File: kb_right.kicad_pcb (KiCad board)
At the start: 2 copper layers, 3.4 x 3 mm, 171 parts, among them J1 10029449-001RLF, SW0 RotaryEncoder_Switch

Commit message: added smd caps
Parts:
- C101, C102, C103, C104, C105, C106, C107, C108, C109, C110, C111, C112, C113, C114, C115, C116, C117, C118, C119, C120, C121, C122, C123, C124, C125, C126, C127, C128, C129, C130, C131, C132, C133, C134, C135, C136, C137, C138, C139, C140, C141, C142, D0, D1, D10, D101, D102, D103, D104, D105, D106, D107, D108, D109, D11, D110, D111, D112, D113, D114, D115, D116, D117, D118, D119, D12, D120, D121, D122, D123, D124, D125, D126, D127, D128, D129, D13, D130, D131, D132, D133, D134, D135, D136, D137, D138, D139, D14, D140, D141, D142, D15, D16, D17, D18, D19, D2, D20, D21, D22, D23, D24, D25, D26, D27, D28, D29, D3, D30, D31, D32, D33, D34, D35, D36, D37, D38, D39, D4, D40, D41, D42, D5, D6, D7, D8, D9: moved to B.Cu
- moved C101 508.5 mm to (27.8, 77.8), turned to -90 degrees
- moved C128 503.6 mm to (32.5, 134.9), turned to -90 degrees
- moved D9 476.8 mm to (30.2, 94.5), turned to 90 degrees
- moved D28 474.9 mm to (63.5, 132.6), turned to 90 degrees
- moved C135 466.6 mm to (36.5, 154.0), turned to -90 degrees
- moved C120 465.9 mm to (41.3, 115.9), turned to -90 degrees
- moved C111 456.5 mm to (55.6, 96.8), turned to -90 degrees
- moved D36 453.8 mm to (75.4, 151.6), turned to 90 degrees
- moved C109 449.3 mm to (18.3, 94.5), turned to 90 degrees
- moved C138 447.9 mm to (110.3, 154.0), turned to -90 degrees
- moved C102 446.2 mm to (46.0, 77.8), turned to -90 degrees
- moved C119 444.2 mm to (23.0, 113.5), turned to 90 degrees
- moved D3 434.0 mm to (77.8, 75.4), turned to 90 degrees
- moved D18 427.0 mm to (34.9, 113.5), turned to 90 degrees
- moved D12 425.5 mm to (87.3, 94.5), turned to 90 degrees
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
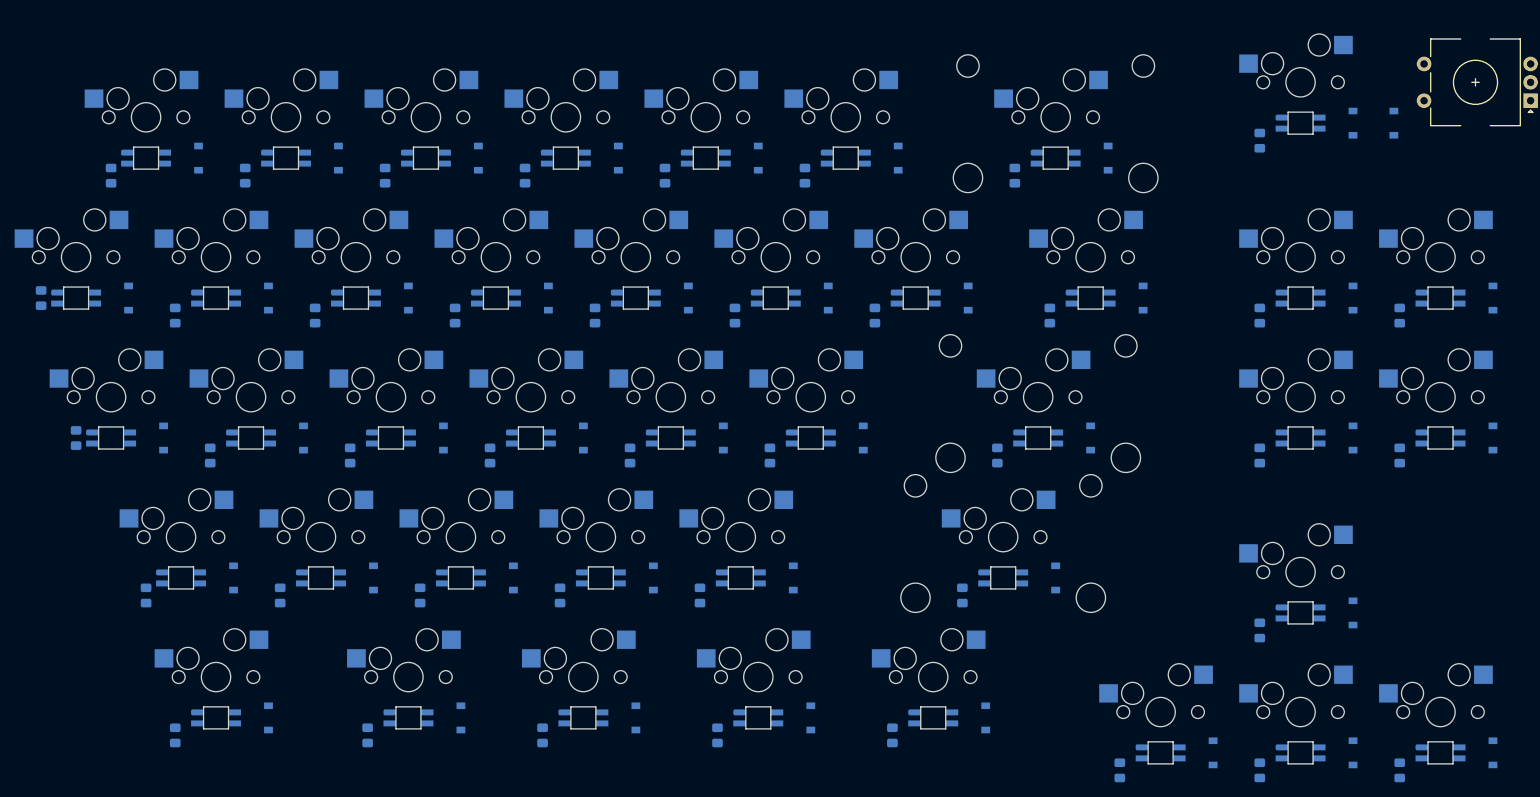
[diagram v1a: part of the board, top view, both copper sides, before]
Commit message: routed matrix
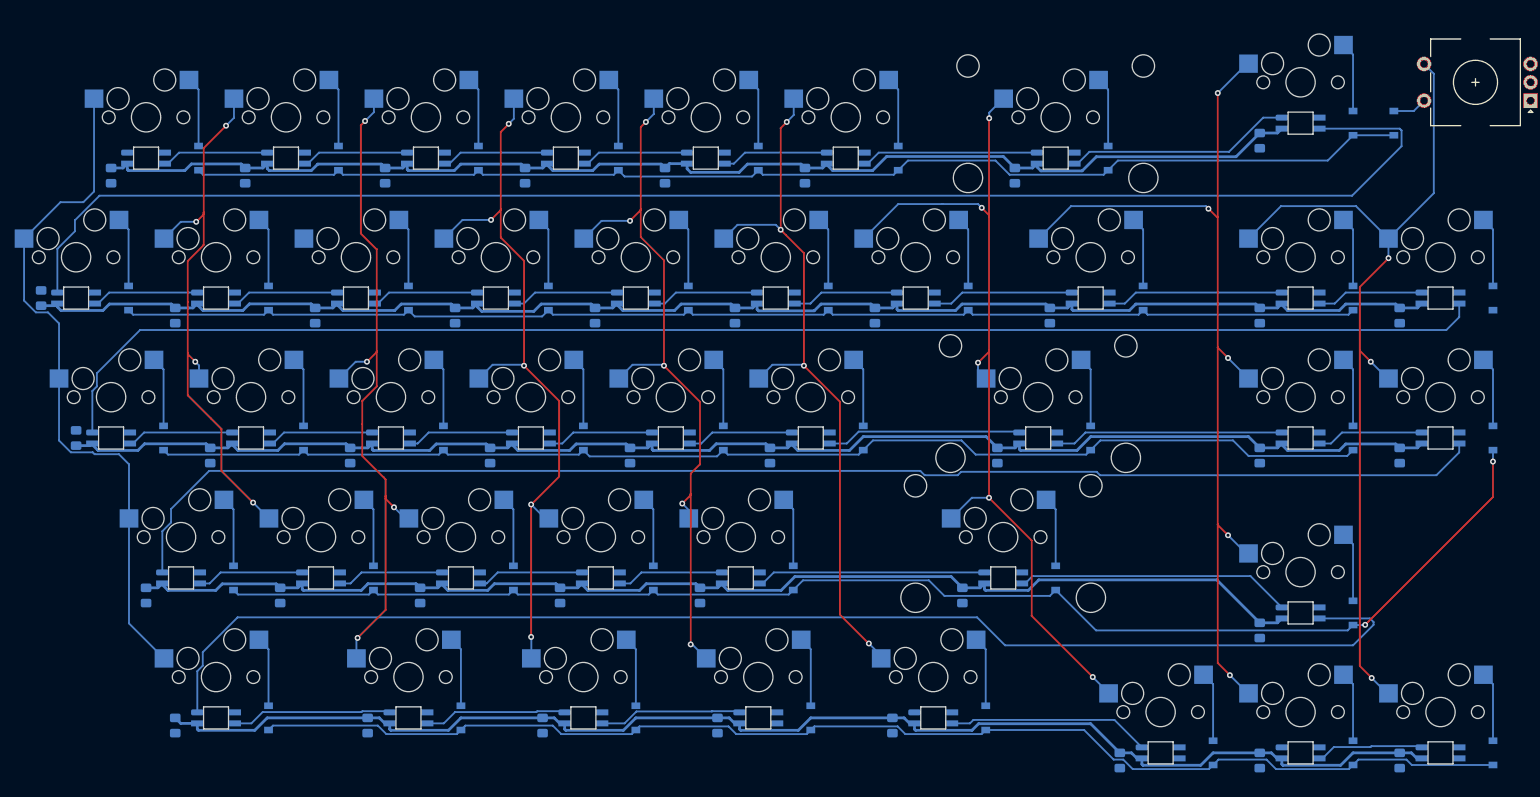
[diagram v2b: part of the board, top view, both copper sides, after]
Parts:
- moved C135 1.34 mm to (36.5, 152.6)
- moved C136 1.34 mm to (62.7, 152.6)
- moved C137 1.34 mm to (86.5, 152.6)
- moved C138 1.34 mm to (110.3, 152.6)
- moved C139 1.34 mm to (134.1, 152.6)
- moved C140 1.34 mm to (165.1, 157.4)
- moved C141 1.34 mm to (184.2, 157.4)
- moved C142 1.34 mm to (203.2, 157.4)
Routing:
- net +5V: track 0.00 -> 922.4 mm
- net Net-(D108-Pad1): track 0.00 -> 209.0 mm
- net Net-(D118-Pad1): track 0.00 -> 198.8 mm
- net /ROW8: track 0.00 -> 191.4 mm, vias 0 -> 2
- net Net-(D127-Pad1): track 0.00 -> 189.8 mm
- net Net-(D134-Pad1): track 0.00 -> 180.6 mm
- net /ROW9: track 0.00 -> 174.5 mm
- net /ROW6: track 0.00 -> 170.9 mm
- net /ROW5: track 0.00 -> 169.0 mm
- net /ROW7: track 0.00 -> 168.0 mm
- net /COL7: track 0.00 -> 128.1 mm, vias 0 -> 5
- net /COL8: track 0.00 -> 120.4 mm, vias 0 -> 3
- net /COL6: track 0.00 -> 119.6 mm, vias 0 -> 5
- net /COL4: track 0.00 -> 102.4 mm, vias 0 -> 5
- net /COL3: track 0.00 -> 101.5 mm, vias 0 -> 5
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
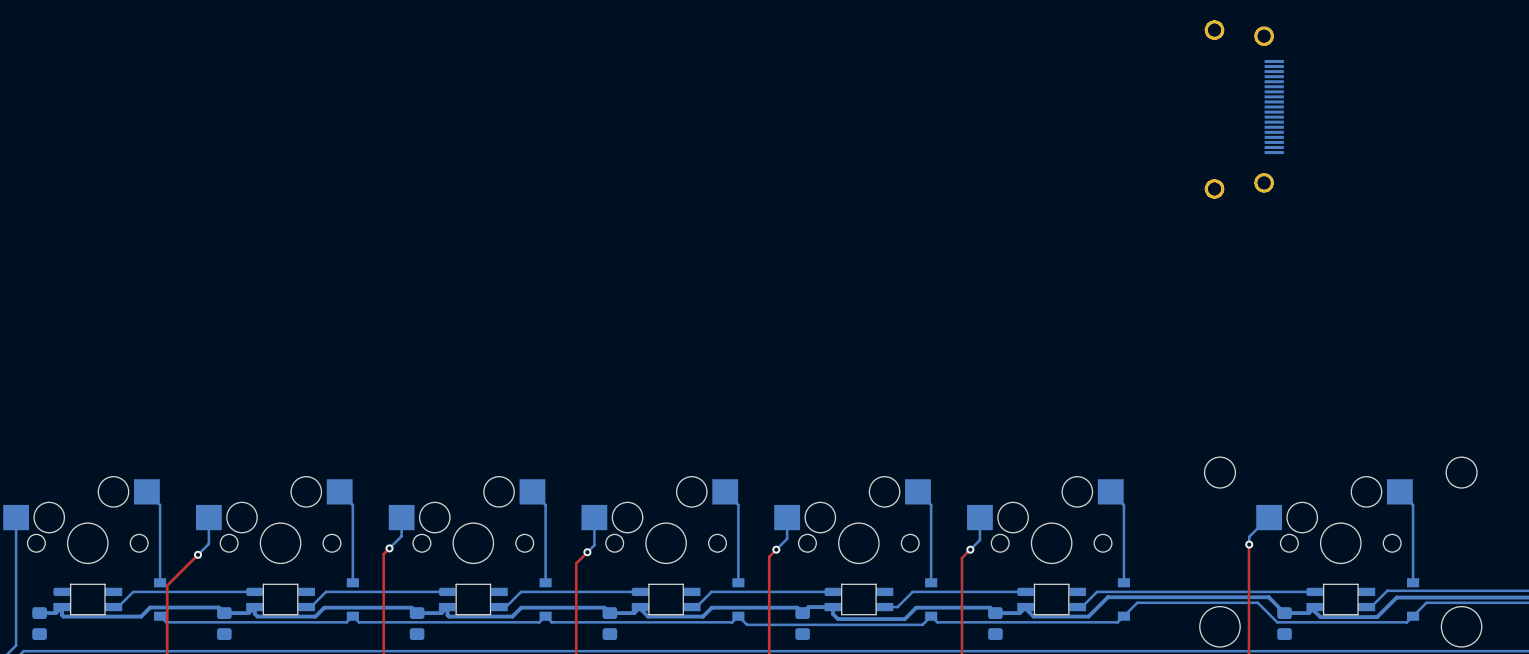
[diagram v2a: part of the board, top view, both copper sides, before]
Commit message: labelled hdmi port
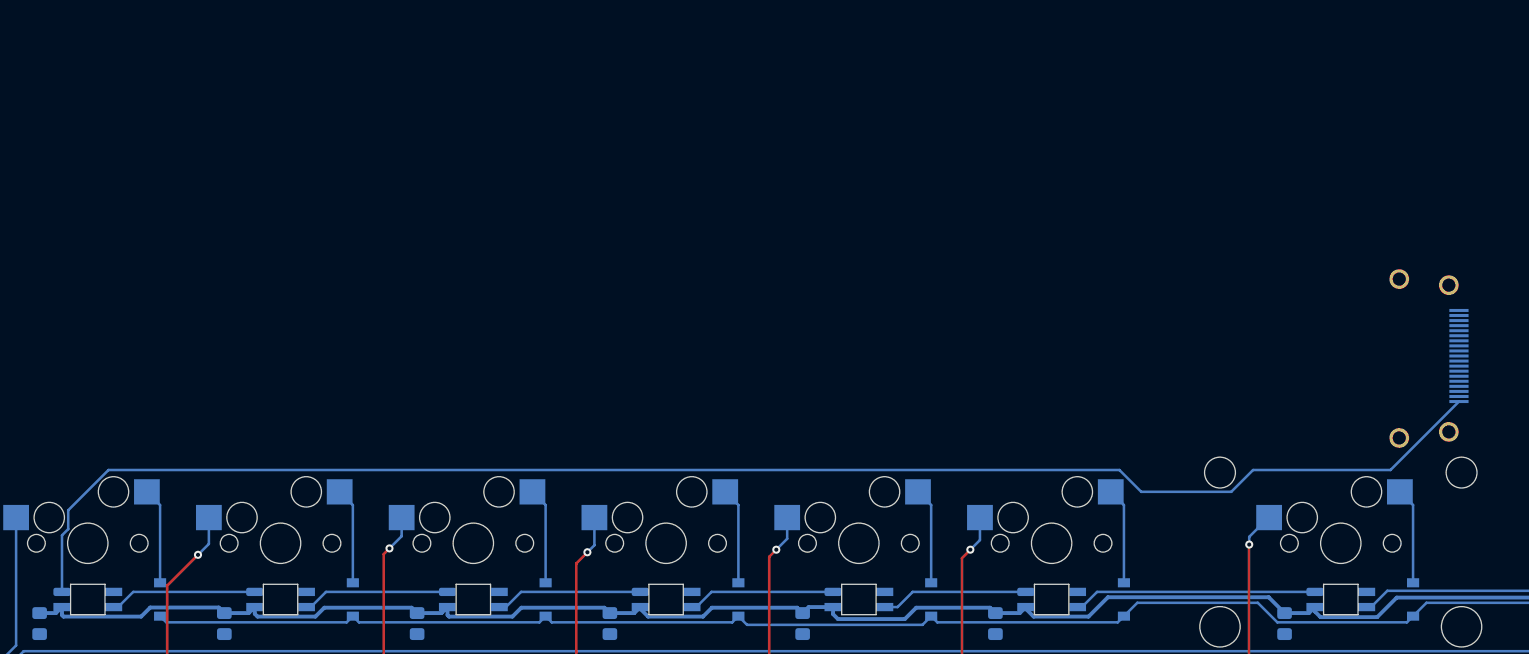
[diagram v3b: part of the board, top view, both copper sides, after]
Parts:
- moved J1 30.6 mm to (167.0, 51.6)
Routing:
- net /RGB_IN: track 0.00 -> 152.0 mm
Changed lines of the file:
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@@
   )
   (footprint "10029449-001RLF:AMPHENOL_10029449-001RLF" (layer "B.Cu")
-    (at 148.7905 26.9875 90)
+    (at 167.04675 51.59375 90)
     (property "MF" "Amphenol")
     (property "PARTREV" "V")
@@
   (segment (start 35.53375 76.15625) (end 37.03375 74.65625) (width 0.25) (layer "B.Cu") (net 50))
   (segment (start 35.09375 76.15625) (end 35.53375 76.15625) (width 0.25) (layer "B.Cu") (net 50))
+  (segment (start 136.647521 64.765521) (end 134.493 62.611) (width 0.254) (layer "B.Cu") (net 51))
+  (segment (start 30.610271 68.449729) (end 29.99375 69.06625) (width 0.254) (layer "B.Cu") (net 51))
+  (segment (start 145.546479 64.765521) (end 136.647521 64.765521) (width 0.254) (layer "B.Cu") (net 51))
+  (segment (start 161.2795 62.611) (end 147.701 62.611) (width 0.254) (layer "B.Cu") (net 51))
+  (segment (start 30.610271 66.589676) (end 30.610271 68.449729) (width 0.254) (layer "B.Cu") (net 51))
+  (segment (start 29.99375 69.06625) (end 29.99375 74.65625) (width 0.254) (layer "B.Cu") (net 51))
+  (segment (start 147.701 62.611) (end 145.546479 64.765521) (width 0.254) (layer "B.Cu") (net 51))
+  (segment (start 134.493 62.611) (end 34.588947 62.611) (width 0.254) (layer "B.Cu") (net 51))
+  (segment (start 168.04675 55.84375) (end 161.2795 62.611) (width 0.254) (layer "B.Cu") (net 51))
+  (segment (start 34.588947 62.611) (end 30.610271 66.589676) (width 0.254) (layer "B.Cu") (net 51))
   (segment (start 56.08375 74.65625) (end 68.09375 74.65625) (width 0.254) (layer "B.Cu") (net 52))
   (segment (start 54.14375 76.15625) (end 54.58375 76.15625) (width 0.254) (layer "B.Cu") (net 52))

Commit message: most routing done
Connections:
- J1 pad 1: unconnected-(J1-Pad1) -> /ROW9
- J1 pad 10: unconnected-(J1-Pad10) -> /COL4
- J1 pad 11: unconnected-(J1-Pad11) -> /COL5
- J1 pad 12: unconnected-(J1-Pad12) -> /COL6
- J1 pad 13: unconnected-(J1-Pad13) -> /COL7
- J1 pad 14: unconnected-(J1-Pad14) -> /COL8
- J1 pad 2: unconnected-(J1-Pad2) -> /ROW8
- J1 pad 3: unconnected-(J1-Pad3) -> /ROW7
- J1 pad 4: unconnected-(J1-Pad4) -> /ROW6
- J1 pad 5: unconnected-(J1-Pad5) -> /ROW5
- J1 pad 6: unconnected-(J1-Pad6) -> /COL0
- J1 pad 7: unconnected-(J1-Pad7) -> /COL1
- J1 pad 8: unconnected-(J1-Pad8) -> /COL2
- J1 pad 9: unconnected-(J1-Pad9) -> /COL3
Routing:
- net /COL0: track 94.5 -> 249.0 mm
- net /COL1: track 75.4 -> 212.7 mm, vias 4 -> 5
- net /ROW9: track 174.5 -> 292.5 mm, vias 0 -> 2
- net /COL2: track 93.0 -> 210.0 mm, vias 4 -> 5
- net /COL3: track 101.5 -> 206.9 mm, vias 5 -> 6
- net /ROW8: track 191.4 -> 288.7 mm, vias 2 -> 4
- net /COL4: track 102.4 -> 188.7 mm, vias 5 -> 6
- net /ROW7: track 168.0 -> 238.8 mm, vias 0 -> 2
- net /COL5: track 98.4 -> 165.4 mm, vias 4 -> 5
- net /ENC_R2: track 0.00 -> 60.3 mm
- net /ENC_R1: track 0.00 -> 58.7 mm
- net /ROW6: track 170.9 -> 222.8 mm, vias 0 -> 2
- net /COL8: track 120.4 -> 164.2 mm, vias 3 -> 4
- net /COL6: track 119.6 -> 159.8 mm, vias 5 -> 6
- net /ROW5: track 169.0 -> 199.8 mm, vias 0 -> 2
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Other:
- board size 3.4 x 3 mm -> 208.8 x 117.5 mm

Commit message: tearing up tracks to fix sk6812
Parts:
- moved C138 26.6 mm to (136.2, 146.5)
- moved C106 26.6 mm to (148.1, 71.7)
- moved D114 26.6 mm to (144.1, 88.3)
- moved D13 26.6 mm to (132.2, 88.3)
- moved MX14 26.6 mm to (144.1, 82.8)
- moved C120 26.6 mm to (67.2, 109.8)
- moved MX11 26.6 mm to (87.0, 82.8)
- moved D10 26.6 mm to (75.1, 88.3)
- moved D111 26.6 mm to (87.0, 88.3)
- moved D18 26.6 mm to (60.8, 107.4)
- moved D35 26.6 mm to (75.1, 145.5)
- moved MX9 26.6 mm to (48.9, 82.8)
- moved C108 26.6 mm to (210.0, 66.9)
- moved C110 26.6 mm to (62.4, 90.7)
- moved C111 26.6 mm to (81.4, 90.7)
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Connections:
- D101 pad 1: Net-(D101-Pad1) -> +5V
- D101 pad 2: GND -> Net-(D101-Pad2)
- D101 pad 3: /RGB_IN -> GND
- D101 pad 4: +5V -> /RGB_IN
- D102 pad 1: Net-(D102-Pad1) -> +5V
- D102 pad 2: GND -> Net-(D102-Pad2)
- D102 pad 3: Net-(D101-Pad1) -> GND
- D102 pad 4: +5V -> Net-(D101-Pad2)
- D103 pad 1: Net-(D103-Pad1) -> +5V
- D103 pad 2: GND -> Net-(D103-Pad2)
- D103 pad 3: Net-(D102-Pad1) -> GND
- D103 pad 4: +5V -> Net-(D102-Pad2)
- D104 pad 1: Net-(D104-Pad1) -> +5V
- D104 pad 2: GND -> Net-(D104-Pad2)
- D104 pad 3: Net-(D103-Pad1) -> GND
- D104 pad 4: +5V -> Net-(D103-Pad2)
- D105 pad 1: Net-(D105-Pad1) -> +5V
- D105 pad 2: GND -> Net-(D105-Pad2)
- D105 pad 3: Net-(D104-Pad1) -> GND
- D105 pad 4: +5V -> Net-(D104-Pad2)
- D106 pad 1: Net-(D106-Pad1) -> +5V
- D106 pad 2: GND -> Net-(D106-Pad2)
- D106 pad 3: Net-(D105-Pad1) -> GND
- D106 pad 4: +5V -> Net-(D105-Pad2)
- D107 pad 1: Net-(D107-Pad1) -> +5V
- D107 pad 2: GND -> Net-(D107-Pad2)
- D107 pad 3: Net-(D106-Pad1) -> GND
- D107 pad 4: +5V -> Net-(D106-Pad2)
- D108 pad 1: Net-(D108-Pad1) -> +5V
- D108 pad 2: GND -> Net-(D108-Pad2)
- D108 pad 3: Net-(D107-Pad1) -> GND
- D108 pad 4: +5V -> Net-(D107-Pad2)
- D109 pad 1: Net-(D109-Pad1) -> +5V
- D109 pad 2: GND -> Net-(D109-Pad2)
- D109 pad 3: Net-(D108-Pad1) -> GND
- D109 pad 4: +5V -> Net-(D108-Pad2)
- D110 pad 1: Net-(D110-Pad1) -> +5V
- D110 pad 2: GND -> Net-(D110-Pad2)
- D110 pad 3: Net-(D109-Pad1) -> GND
- D110 pad 4: +5V -> Net-(D109-Pad2)
- D111 pad 1: Net-(D111-Pad1) -> +5V
- D111 pad 2: GND -> Net-(D111-Pad2)
- D111 pad 3: Net-(D110-Pad1) -> GND
- D111 pad 4: +5V -> Net-(D110-Pad2)
- D112 pad 1: Net-(D112-Pad1) -> +5V
- D112 pad 2: GND -> Net-(D112-Pad2)
- D112 pad 3: Net-(D111-Pad1) -> GND
- D112 pad 4: +5V -> Net-(D111-Pad2)
- D113 pad 1: Net-(D113-Pad1) -> +5V
- D113 pad 2: GND -> Net-(D113-Pad2)
- D113 pad 3: Net-(D112-Pad1) -> GND
- D113 pad 4: +5V -> Net-(D112-Pad2)
- D114 pad 1: Net-(D114-Pad1) -> +5V
- D114 pad 2: GND -> Net-(D114-Pad2)
- D114 pad 3: Net-(D113-Pad1) -> GND
- D114 pad 4: +5V -> Net-(D113-Pad2)
- D115 pad 1: Net-(D115-Pad1) -> +5V
- D115 pad 2: GND -> Net-(D115-Pad2)
- D115 pad 3: Net-(D114-Pad1) -> GND
- D115 pad 4: +5V -> Net-(D114-Pad2)
- D116 pad 1: Net-(D116-Pad1) -> +5V
- D116 pad 2: GND -> Net-(D116-Pad2)
- D116 pad 3: Net-(D115-Pad1) -> GND
- D116 pad 4: +5V -> Net-(D115-Pad2)
- D117 pad 1: Net-(D117-Pad1) -> +5V
- D117 pad 2: GND -> Net-(D117-Pad2)
- D117 pad 3: Net-(D116-Pad1) -> GND
- D117 pad 4: +5V -> Net-(D116-Pad2)
- D118 pad 1: Net-(D118-Pad1) -> +5V
- D118 pad 2: GND -> Net-(D118-Pad2)
- D118 pad 3: Net-(D117-Pad1) -> GND
- D118 pad 4: +5V -> Net-(D117-Pad2)
- D119 pad 1: Net-(D119-Pad1) -> +5V
- D119 pad 2: GND -> Net-(D119-Pad2)
- D119 pad 3: Net-(D118-Pad1) -> GND
- D119 pad 4: +5V -> Net-(D118-Pad2)
- D120 pad 1: Net-(D120-Pad1) -> +5V
- D120 pad 2: GND -> Net-(D120-Pad2)
- D120 pad 3: Net-(D119-Pad1) -> GND
- D120 pad 4: +5V -> Net-(D119-Pad2)
- D121 pad 1: Net-(D121-Pad1) -> +5V
- D121 pad 2: GND -> Net-(D121-Pad2)
- D121 pad 3: Net-(D120-Pad1) -> GND
- D121 pad 4: +5V -> Net-(D120-Pad2)
- D122 pad 1: Net-(D122-Pad1) -> +5V
- D122 pad 2: GND -> Net-(D122-Pad2)
- D122 pad 3: Net-(D121-Pad1) -> GND
- D122 pad 4: +5V -> Net-(D121-Pad2)
- D123 pad 1: Net-(D123-Pad1) -> +5V
- D123 pad 2: GND -> Net-(D123-Pad2)
- D123 pad 3: Net-(D122-Pad1) -> GND
- D123 pad 4: +5V -> Net-(D122-Pad2)
- D124 pad 1: Net-(D124-Pad1) -> +5V
- D124 pad 2: GND -> Net-(D124-Pad2)
- D124 pad 3: Net-(D123-Pad1) -> GND
- D124 pad 4: +5V -> Net-(D123-Pad2)
- D125 pad 1: Net-(D125-Pad1) -> +5V
- D125 pad 2: GND -> Net-(D125-Pad2)
- D125 pad 3: Net-(D124-Pad1) -> GND
- D125 pad 4: +5V -> Net-(D124-Pad2)
- D126 pad 1: Net-(D126-Pad1) -> +5V
- D126 pad 2: GND -> Net-(D126-Pad2)
- D126 pad 3: Net-(D125-Pad1) -> GND
- D126 pad 4: +5V -> Net-(D125-Pad2)
- D127 pad 1: Net-(D127-Pad1) -> +5V
- D127 pad 2: GND -> Net-(D127-Pad2)
- D127 pad 3: Net-(D126-Pad1) -> GND
- D127 pad 4: +5V -> Net-(D126-Pad2)
- D128 pad 1: Net-(D128-Pad1) -> +5V
- D128 pad 2: GND -> Net-(D128-Pad2)
- D128 pad 3: Net-(D127-Pad1) -> GND
- D128 pad 4: +5V -> Net-(D127-Pad2)
- D129 pad 1: Net-(D129-Pad1) -> +5V
- D129 pad 2: GND -> Net-(D129-Pad2)
- D129 pad 3: Net-(D128-Pad1) -> GND
- D129 pad 4: +5V -> Net-(D128-Pad2)
- D130 pad 1: Net-(D130-Pad1) -> +5V
- D130 pad 2: GND -> Net-(D130-Pad2)
- D130 pad 3: Net-(D129-Pad1) -> GND
- D130 pad 4: +5V -> Net-(D129-Pad2)
- D131 pad 1: Net-(D131-Pad1) -> +5V
- D131 pad 2: GND -> Net-(D131-Pad2)
- D131 pad 3: Net-(D130-Pad1) -> GND
- D131 pad 4: +5V -> Net-(D130-Pad2)
- D132 pad 1: Net-(D132-Pad1) -> +5V
- D132 pad 2: GND -> Net-(D132-Pad2)
- D132 pad 3: Net-(D131-Pad1) -> GND
- D132 pad 4: +5V -> Net-(D131-Pad2)
- D133 pad 1: Net-(D133-Pad1) -> +5V
- D133 pad 2: GND -> Net-(D133-Pad2)
- D133 pad 3: Net-(D132-Pad1) -> GND
- D133 pad 4: +5V -> Net-(D132-Pad2)
- D134 pad 1: Net-(D134-Pad1) -> +5V
- D134 pad 2: GND -> Net-(D134-Pad2)
- D134 pad 3: Net-(D133-Pad1) -> GND
- D134 pad 4: +5V -> Net-(D133-Pad2)
- D135 pad 1: Net-(D135-Pad1) -> +5V
- D135 pad 2: GND -> Net-(D135-Pad2)
- D135 pad 3: Net-(D134-Pad1) -> GND
- D135 pad 4: +5V -> Net-(D134-Pad2)
- D136 pad 1: Net-(D136-Pad1) -> +5V
- D136 pad 2: GND -> Net-(D136-Pad2)
- D136 pad 3: Net-(D135-Pad1) -> GND
- D136 pad 4: +5V -> Net-(D135-Pad2)
- D137 pad 1: Net-(D137-Pad1) -> +5V
- D137 pad 2: GND -> Net-(D137-Pad2)
- D137 pad 3: Net-(D136-Pad1) -> GND
- D137 pad 4: +5V -> Net-(D136-Pad2)
- D138 pad 1: Net-(D138-Pad1) -> +5V
- D138 pad 2: GND -> Net-(D138-Pad2)
- D138 pad 3: Net-(D137-Pad1) -> GND
- D138 pad 4: +5V -> Net-(D137-Pad2)
- D139 pad 1: Net-(D139-Pad1) -> +5V
- D139 pad 2: GND -> Net-(D139-Pad2)
- D139 pad 3: Net-(D138-Pad1) -> GND
- D139 pad 4: +5V -> Net-(D138-Pad2)
- D140 pad 1: Net-(D140-Pad1) -> +5V
- D140 pad 2: GND -> Net-(D140-Pad2)
- D140 pad 3: Net-(D139-Pad1) -> GND
- D140 pad 4: +5V -> Net-(D139-Pad2)
- D141 pad 1: Net-(D141-Pad1) -> +5V
- D141 pad 2: GND -> Net-(D141-Pad2)
- D141 pad 3: Net-(D140-Pad1) -> GND
- D141 pad 4: +5V -> Net-(D140-Pad2)
- D142 pad 1: unconnected-(D142-Pad1) -> +5V
- D142 pad 2: GND -> unconnected-(D142-Pad2)
- D142 pad 3: Net-(D141-Pad1) -> GND
- D142 pad 4: +5V -> Net-(D141-Pad2)
- J1 pad 15: /ENC_R1 -> /ENC_R2
- J1 pad 16: /ENC_R2 -> /ENC_R1
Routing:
- net +5V: track 922.4 -> 1892.9 mm, vias 0 -> 6
- net GND: track 0.00 -> 410.0 mm, vias 0 -> 140
- net Net-(D108-Pad1): track 209.0 -> 0.00 mm
- net Net-(D118-Pad1): track 198.8 -> 0.00 mm
- net Net-(D127-Pad1): track 189.8 -> 0.00 mm
- net Net-(D134-Pad1): track 180.6 -> 0.00 mm
- net Net-(D133-Pad1): track 37.6 -> 0.00 mm
- net Net-(D132-Pad1): track 31.2 -> 0.00 mm
- net Net-(D125-Pad1): track 31.2 -> 0.00 mm
- net /ROW7: track 238.8 -> 269.7 mm, vias 2 -> 4
- net Net-(D107-Pad1): track 30.8 -> 0.00 mm
- net Net-(D139-Pad1): track 27.6 -> 0.00 mm
- net Net-(D124-Pad1): track 26.6 -> 0.00 mm
- net Net-(D106-Pad1): track 24.7 -> 0.00 mm
- net Net-(D116-Pad1): track 24.1 -> 0.00 mm
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- added copper zone on B.Cu, net GND
- added copper zone on F.Cu, net GND
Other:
- outline, holes or cut-outs redrawn
